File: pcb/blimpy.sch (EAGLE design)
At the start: 91 parts, among them J4 3-PIN SMD, J5 3-PIN SMD, J6 3-PIN SMD, J7 3-PIN SMD, Q1 mmbt2222, Q2 mmbt2222, Q3 DMG3415U, U1 RGB, U10 MAX17048, U2 AP2112-3.3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

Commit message: updated
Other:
- note added: "Blimpy Board 1.0 Immersive Art Space ZHdK - Joël Gähwiler"
- note removed: "TODO - Check all components"
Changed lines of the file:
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@@
 I2C Address: 0x4A</text>
 <text x="378.46" y="185.42" size="1.27" layer="97">INT OSC</text>
-<text x="160.02" y="-58.42" size="5.08" layer="94" align="top-left">TODO
-- Check all components</text>
 <text x="342.9" y="106.68" size="1.778" layer="94">GPIO Expander 1
 I2C Address: 0x3E</text>
@@
 <text x="45.72" y="-50.8" size="1.778" layer="94">SERVOS</text>
 <text x="462.28" y="228.6" size="1.778" layer="94">MOTORS</text>
+<text x="129.54" y="-119.38" size="12.7" layer="95">Blimpy Board 1.0
+Immersive Art Space
+ZHdK - Joël Gähwiler</text>
 </plain>
 <instances>

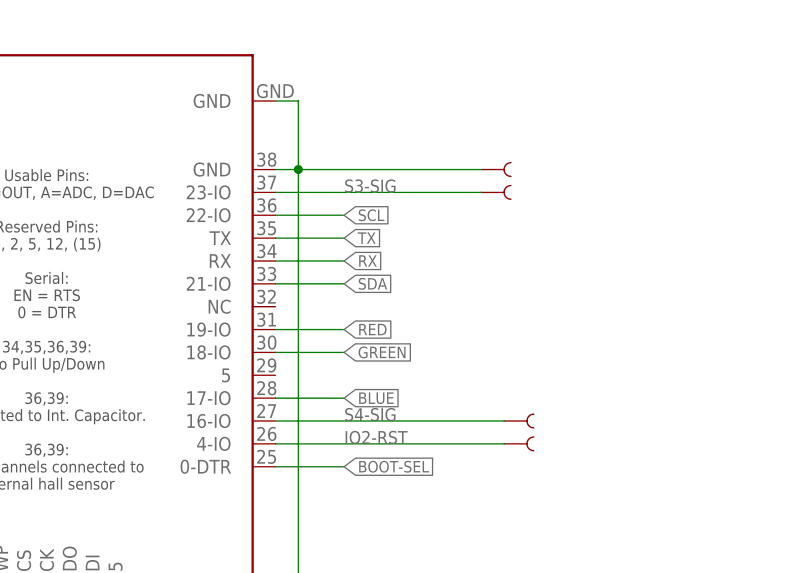
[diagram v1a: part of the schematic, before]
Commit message: added more pogo pins
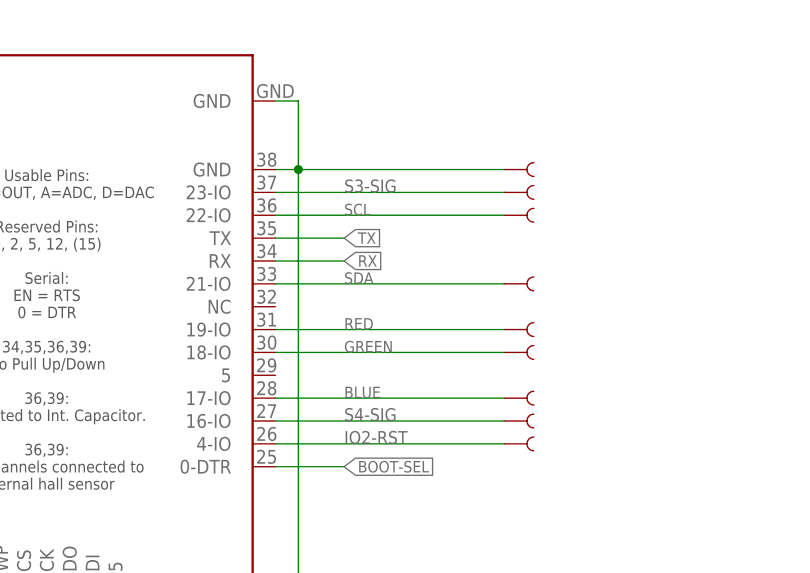
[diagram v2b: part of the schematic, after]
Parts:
- added TP18, TP19, TP20, TP21, TP22: TEST-POINT3, SparkFun-Connectors:TEST-POINT3
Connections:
- net BLUE: now also TP22.1
- net GREEN: now also TP21.1
- net RED: now also TP20.1
- net SCL: now also TP18.1
- net SDA: now also TP19.1
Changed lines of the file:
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@@
 <part name="TP16" library="SparkFun-Connectors" library_urn="urn:adsk.eagle:library:513" deviceset="TEST-POINT" device="3" package3d_urn="urn:adsk.eagle:package:38286/1" value="TEST-POINT3"/>
 <part name="TP17" library="SparkFun-Connectors" library_urn="urn:adsk.eagle:library:513" deviceset="TEST-POINT" device="3" package3d_urn="urn:adsk.eagle:package:38286/1" value="TEST-POINT3"/>
+<part name="TP18" library="SparkFun-Connectors" library_urn="urn:adsk.eagle:library:513" deviceset="TEST-POINT" device="3" package3d_urn="urn:adsk.eagle:package:38286/1" value="TEST-POINT3"/>
+<part name="TP19" library="SparkFun-Connectors" library_urn="urn:adsk.eagle:library:513" deviceset="TEST-POINT" device="3" package3d_urn="urn:adsk.eagle:package:38286/1" value="TEST-POINT3"/>
+<part name="TP20" library="SparkFun-Connectors" library_urn="urn:adsk.eagle:library:513" deviceset="TEST-POINT" device="3" package3d_urn="urn:adsk.eagle:package:38286/1" value="TEST-POINT3"/>
+<part name="TP21" library="SparkFun-Connectors" library_urn="urn:adsk.eagle:library:513" deviceset="TEST-POINT" device="3" package3d_urn="urn:adsk.eagle:package:38286/1" value="TEST-POINT3"/>
+<part name="TP22" library="SparkFun-Connectors" library_urn="urn:adsk.eagle:library:513" deviceset="TEST-POINT" device="3" package3d_urn="urn:adsk.eagle:package:38286/1" value="TEST-POINT3"/>
 </parts>
 <sheets>
@@
 <instance part="TP11" gate="G$1" x="152.4" y="27.94" smashed="yes" rot="R180"/>
 <instance part="TP12" gate="G$1" x="152.4" y="30.48" smashed="yes" rot="R180"/>
-<instance part="TP13" gate="G$1" x="248.92" y="30.48" smashed="yes"/>
-<instance part="TP14" gate="G$1" x="248.92" y="27.94" smashed="yes"/>
+<instance part="TP13" gate="G$1" x="251.46" y="30.48" smashed="yes"/>
+<instance part="TP14" gate="G$1" x="251.46" y="27.94" smashed="yes"/>
 <instance part="TP15" gate="G$1" x="251.46" y="2.54" smashed="yes"/>
 <instance part="TP16" gate="G$1" x="251.46" y="0" smashed="yes"/>
 <instance part="TP17" gate="G$1" x="190.5" y="-40.64" smashed="yes" rot="R270"/>
+<instance part="TP18" gate="G$1" x="251.46" y="25.4" smashed="yes"/>
+<instance part="TP19" gate="G$1" x="251.46" y="17.78" smashed="yes"/>
+<instance part="TP20" gate="G$1" x="251.46" y="12.7" smashed="yes"/>
+<instance part="TP21" gate="G$1" x="251.46" y="10.16" smashed="yes"/>
+<instance part="TP22" gate="G$1" x="251.46" y="5.08" smashed="yes"/>
 </instances>
 <busses>
@@
 <junction x="170.18" y="30.48"/>
 <pinref part="TP13" gate="G$1" pin="1"/>
-<wire x1="228.6" y1="30.48" x2="248.92" y2="30.48" width="0.1524" layer="91"/>
+<wire x1="228.6" y1="30.48" x2="251.46" y2="30.48" width="0.1524" layer="91"/>
 </segment>
 <segment>
@@
 <segment>
 <pinref part="U9" gate="G$1" pin="19-IO"/>
-<wire x1="226.06" y1="12.7" x2="233.68" y2="12.7" width="0.1524" layer="91"/>
-<label x="233.68" y="12.7" size="1.27" layer="95" xref="yes"/>
+<label x="233.68" y="12.7" size="1.27" layer="95"/>
+<pinref part="TP20" gate="G$1" pin="1"/>
+<wire x1="226.06" y1="12.7" x2="251.46" y2="12.7" width="0.1524" layer="91"/>
 </segment>
 </net>
@@
 <segment>
 <pinref part="U9" gate="G$1" pin="18-IO"/>
-<wire x1="226.06" y1="10.16" x2="233.68" y2="10.16" width="0.1524" layer="91"/>
-<label x="233.68" y="10.16" size="1.27" layer="95" xref="yes"/>
+<label x="233.68" y="10.16" size="1.27" layer="95"/>
+<pinref part="TP21" gate="G$1" pin="1"/>
+<wire x1="226.06" y1="10.16" x2="251.46" y2="10.16" width="0.1524" layer="91"/>
 </segment>
 </net>
@@
 <segment>
 <pinref part="U9" gate="G$1" pin="17-IO"/>
-<wire x1="226.06" y1="5.08" x2="233.68" y2="5.08" width="0.1524" layer="91"/>
-<label x="233.68" y="5.08" size="1.27" layer="95" xref="yes"/>
+<label x="233.68" y="5.08" size="1.27" layer="95"/>
+<pinref part="TP22" gate="G$1" pin="1"/>
+<wire x1="226.06" y1="5.08" x2="251.46" y2="5.08" width="0.1524" layer="91"/>
 </segment>
 </net>
@@
 <segment>
 <pinref part="U9" gate="G$1" pin="21-IO"/>
-<wire x1="226.06" y1="17.78" x2="233.68" y2="17.78" width="0.1524" layer="91"/>
-<label x="233.68" y="17.78" size="1.27" layer="95" xref="yes"/>
+<label x="233.68" y="17.78" size="1.27" layer="95"/>
+<pinref part="TP19" gate="G$1" pin="1"/>
+<wire x1="226.06" y1="17.78" x2="251.46" y2="17.78" width="0.1524" layer="91"/>
 </segment>
 <segment>
@@
 <segment>
 <pinref part="U9" gate="G$1" pin="22-IO"/>
-<wire x1="226.06" y1="25.4" x2="233.68" y2="25.4" width="0.1524" layer="91"/>
-<label x="233.68" y="25.4" size="1.27" layer="95" xref="yes"/>
+<label x="233.68" y="25.4" size="1.27" layer="95"/>
+<pinref part="TP18" gate="G$1" pin="1"/>
+<wire x1="226.06" y1="25.4" x2="251.46" y2="25.4" width="0.1524" layer="91"/>
 </segment>
 <segment>
@@
 <label x="233.68" y="27.94" size="1.4224" layer="95"/>
 <pinref part="TP14" gate="G$1" pin="1"/>
-<wire x1="226.06" y1="27.94" x2="248.92" y2="27.94" width="0.1524" layer="91"/>
-</segment>
-</net>
+<wire x1="226.06" y1="27.94" x2="251.46" y2="27.94" width="0.1524" layer="91"/>
+</segment>
+</net>

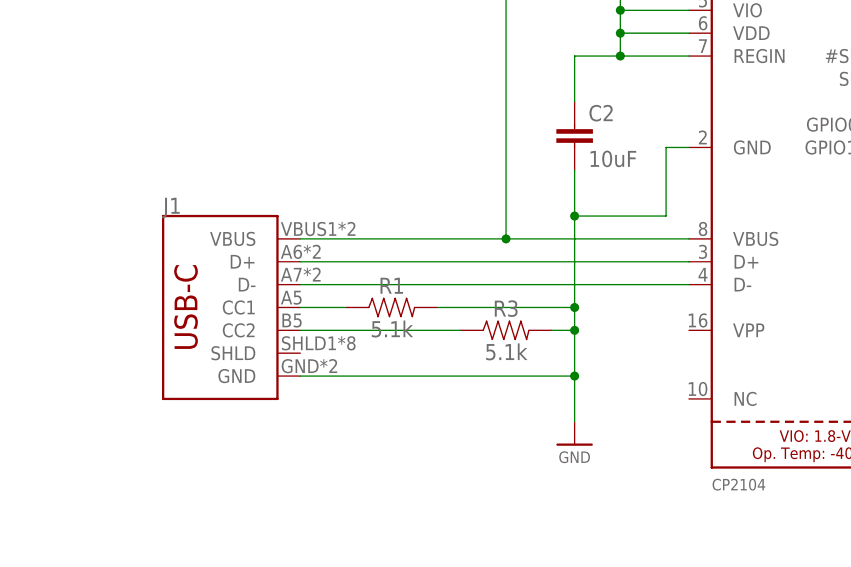
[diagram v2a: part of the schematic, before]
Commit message: switched back to micro usb connector and moved led
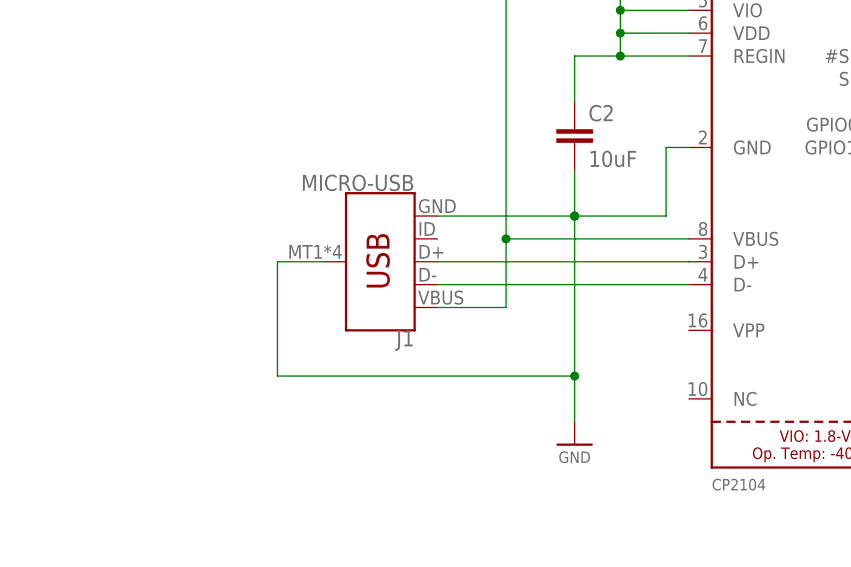
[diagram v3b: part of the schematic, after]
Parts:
- removed R1, R3: 5.1k, SparkFun-Resistors:1KOHM-0603-1/10W-1%
- J1: value (none) -> MICRO-USB; device SparkFun-Connectors:USB_C16PIN -> SparkFun-Connectors:USB_MICRO-B_SMT
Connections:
- removed net N$17: J1.CC2, R3.1
- removed net N$5: J1.CC1, R1.1
- net GND: now also J1.SHIELD; no longer R1.2, R3.2
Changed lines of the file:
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@@
 <part name="U10" library="SparkFun-IC-Power" library_urn="urn:adsk.eagle:library:526" deviceset="MAX17048" device="DFN8" package3d_urn="urn:adsk.eagle:package:39085/1" value="MAX17048"/>
 <part name="C11" library="SparkFun-Capacitors" library_urn="urn:adsk.eagle:library:510" deviceset="0.1UF" device="-0603-25V-5%" package3d_urn="urn:adsk.eagle:package:37414/1" value="0.1uF"/>
-<part name="J1" library="SparkFun-Connectors" deviceset="USB_C" device="16PIN"/>
-<part name="R1" library="SparkFun-Resistors" library_urn="urn:adsk.eagle:library:532" deviceset="1KOHM" device="-0603-1/10W-1%" package3d_urn="urn:adsk.eagle:package:39650/1" value="5.1k"/>
-<part name="R3" library="SparkFun-Resistors" library_urn="urn:adsk.eagle:library:532" deviceset="1KOHM" device="-0603-1/10W-1%" package3d_urn="urn:adsk.eagle:package:39650/1" value="5.1k"/>
 <part name="TP1" library="SparkFun-Connectors" library_urn="urn:adsk.eagle:library:513" deviceset="TEST-POINT" device="3" package3d_urn="urn:adsk.eagle:package:38286/1" value="TEST-POINT3"/>
 <part name="TP2" library="SparkFun-Connectors" library_urn="urn:adsk.eagle:library:513" deviceset="TEST-POINT" device="3" package3d_urn="urn:adsk.eagle:package:38286/1" value="TEST-POINT3"/>
@@
 <part name="TP21" library="SparkFun-Connectors" library_urn="urn:adsk.eagle:library:513" deviceset="TEST-POINT" device="3" package3d_urn="urn:adsk.eagle:package:38286/1" value="TEST-POINT3"/>
 <part name="TP22" library="SparkFun-Connectors" library_urn="urn:adsk.eagle:library:513" deviceset="TEST-POINT" device="3" package3d_urn="urn:adsk.eagle:package:38286/1" value="TEST-POINT3"/>
+<part name="J1" library="SparkFun-Connectors" deviceset="USB_MICRO-B" device="_SMT" value="MICRO-USB"/>
 </parts>
 <sheets>
@@
 <attribute name="VALUE" x="108.204" y="104.521" size="1.778" layer="96" font="vector"/>
 </instance>
-<instance part="J1" gate="J1" x="152.4" y="177.8" smashed="yes">
-<attribute name="VALUE" x="149.86" y="165.354" size="1.778" layer="96" font="vector" rot="MR180" align="top-left"/>
-<attribute name="NAME" x="149.86" y="188.214" size="1.778" layer="95" font="vector"/>
-</instance>
-<instance part="R1" gate="G$1" x="175.26" y="177.8" smashed="yes">
-<attribute name="NAME" x="175.26" y="179.324" size="1.778" layer="95" font="vector" align="bottom-center"/>
-<attribute name="VALUE" x="175.26" y="176.276" size="1.778" layer="96" font="vector" align="top-center"/>
-</instance>
-<instance part="R3" gate="G$1" x="187.96" y="175.26" smashed="yes">
-<attribute name="NAME" x="187.96" y="176.784" size="1.778" layer="95" font="vector" align="bottom-center"/>
-<attribute name="VALUE" x="187.96" y="173.736" size="1.778" layer="96" font="vector" align="top-center"/>
-</instance>
 <instance part="TP1" gate="G$1" x="152.4" y="12.7" smashed="yes" rot="R180"/>
 <instance part="TP2" gate="G$1" x="152.4" y="10.16" smashed="yes" rot="R180"/>
@@
 <instance part="TP21" gate="G$1" x="251.46" y="10.16" smashed="yes"/>
 <instance part="TP22" gate="G$1" x="251.46" y="5.08" smashed="yes"/>
+<instance part="J1" gate="G$1" x="175.26" y="182.88" smashed="yes" rot="R180">
+<attribute name="VALUE" x="177.8" y="190.754" size="1.778" layer="96" font="vector" rot="R180" align="top-left"/>
+<attribute name="NAME" x="177.8" y="175.26" size="1.778" layer="95" font="vector" rot="R180"/>
+</instance>
 </instances>
 <busses>
@@
 <pinref part="C2" gate="G$1" pin="2"/>
 <wire x1="195.58" y1="193.04" x2="195.58" y2="187.96" width="0.1524" layer="91"/>
-<wire x1="195.58" y1="187.96" x2="195.58" y2="177.8" width="0.1524" layer="91"/>
-<wire x1="195.58" y1="177.8" x2="195.58" y2="175.26" width="0.1524" layer="91"/>
-<wire x1="195.58" y1="175.26" x2="195.58" y2="170.18" width="0.1524" layer="91"/>
+<wire x1="195.58" y1="187.96" x2="195.58" y2="170.18" width="0.1524" layer="91"/>
 <wire x1="195.58" y1="170.18" x2="195.58" y2="165.1" width="0.1524" layer="91"/>
 <wire x1="205.74" y1="187.96" x2="195.58" y2="187.96" width="0.1524" layer="91"/>
 <junction x="195.58" y="187.96"/>
 <pinref part="GND9" gate="1" pin="GND"/>
-<pinref part="J1" gate="J1" pin="GND"/>
-<wire x1="165.1" y1="170.18" x2="195.58" y2="170.18" width="0.1524" layer="91"/>
+<wire x1="180.34" y1="187.96" x2="195.58" y2="187.96" width="0.1524" layer="91"/>
+<junction x="195.58" y="187.96"/>
+<pinref part="J1" gate="G$1" pin="GND"/>
+<pinref part="J1" gate="G$1" pin="SHIELD"/>
+<wire x1="167.64" y1="182.88" x2="162.56" y2="182.88" width="0.1524" layer="91"/>
+<wire x1="162.56" y1="182.88" x2="162.56" y2="170.18" width="0.1524" layer="91"/>
+<wire x1="162.56" y1="170.18" x2="195.58" y2="170.18" width="0.1524" layer="91"/>
 <junction x="195.58" y="170.18"/>
-<pinref part="R3" gate="G$1" pin="2"/>
-<wire x1="193.04" y1="175.26" x2="195.58" y2="175.26" width="0.1524" layer="91"/>
-<junction x="195.58" y="175.26"/>
-<pinref part="R1" gate="G$1" pin="2"/>
-<wire x1="180.34" y1="177.8" x2="195.58" y2="177.8" width="0.1524" layer="91"/>
-<junction x="195.58" y="177.8"/>
 </segment>
 <segment>
@@
 <segment>
 <pinref part="U7" gate="G$1" pin="D+"/>
-<pinref part="J1" gate="J1" pin="D+"/>
-<wire x1="208.28" y1="182.88" x2="165.1" y2="182.88" width="0.1524" layer="91"/>
+<wire x1="208.28" y1="182.88" x2="180.34" y2="182.88" width="0.1524" layer="91"/>
+<pinref part="J1" gate="G$1" pin="D+"/>
 </segment>
 </net>
@@
 <segment>
 <pinref part="U7" gate="G$1" pin="D-"/>
-<pinref part="J1" gate="J1" pin="D-"/>
-<wire x1="165.1" y1="180.34" x2="208.28" y2="180.34" width="0.1524" layer="91"/>
+<wire x1="180.34" y1="180.34" x2="208.28" y2="180.34" width="0.1524" layer="91"/>
+<pinref part="J1" gate="G$1" pin="D-"/>
 </segment>
 </net>
@@
 <wire x1="187.96" y1="185.42" x2="208.28" y2="185.42" width="0.1524" layer="91"/>
 <pinref part="SUPPLY1" gate="G$1" pin="V_USB"/>
-<pinref part="J1" gate="J1" pin="VBUS"/>
 <wire x1="187.96" y1="185.42" x2="187.96" y2="215.9" width="0.1524" layer="91"/>
-<wire x1="165.1" y1="185.42" x2="187.96" y2="185.42" width="0.1524" layer="91"/>
 <junction x="187.96" y="185.42"/>
+<wire x1="187.96" y1="185.42" x2="187.96" y2="177.8" width="0.1524" layer="91"/>
+<pinref part="J1" gate="G$1" pin="VBUS"/>
+<wire x1="180.34" y1="177.8" x2="187.96" y2="177.8" width="0.1524" layer="91"/>
 </segment>
 <segment>
@@
 </segment>
 </net>
-<net name="N$5" class="0">
-<segment>
-<pinref part="J1" gate="J1" pin="CC1"/>
-<pinref part="R1" gate="G$1" pin="1"/>
-<wire x1="165.1" y1="177.8" x2="170.18" y2="177.8" width="0.1524" layer="91"/>
-</segment>
-</net>
-<net name="N$17" class="0">
-<segment>
-<pinref part="J1" gate="J1" pin="CC2"/>
-<pinref part="R3" gate="G$1" pin="1"/>
-<wire x1="165.1" y1="175.26" x2="182.88" y2="175.26" width="0.1524" layer="91"/>
-</segment>
-</net>
